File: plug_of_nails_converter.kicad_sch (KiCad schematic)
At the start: 6 parts, among them CN1 5103308-1

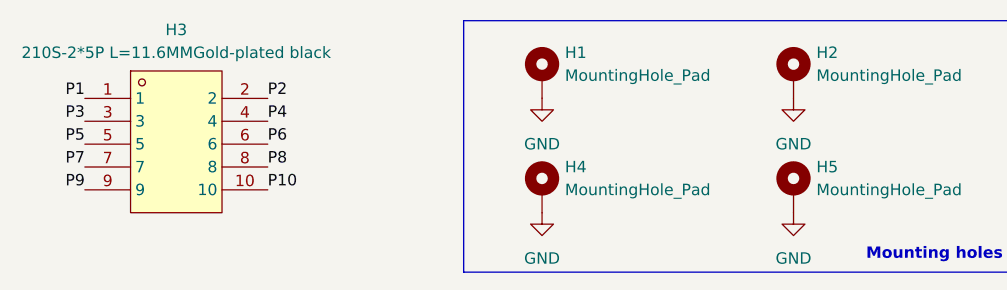
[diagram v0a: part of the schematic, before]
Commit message: Chaning IDC pin numbers and adding bottom CU layer
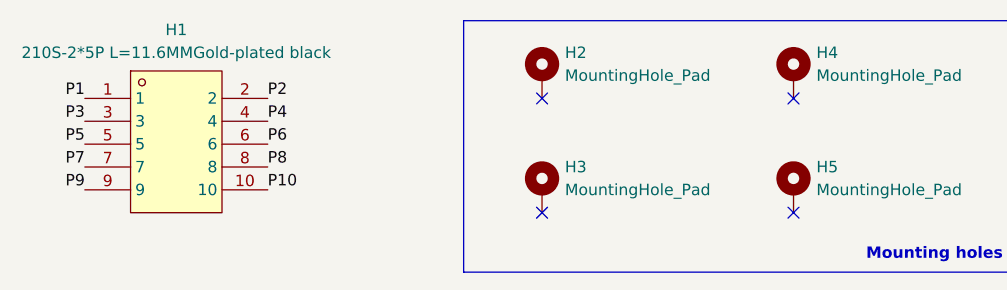
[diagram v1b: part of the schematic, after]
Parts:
- CN1: symbol my_symbol_library:5103308-1 -> pepy_sym_lib:[10P_2X5_IDC_MALE]TE Connectivity 5103308-1
- H1: renamed from H3; symbol my_symbol_library:210S-2*5PL=11.6MMGold-platedblack -> pepy_sym_lib:[10P_HEADER_STR]Ckmtw(Shenzhen Cankemeng) B-2100S10P-B110
- renumbered H1 to H2, H4 to H3, H2 to H4
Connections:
- removed net GND: H2.1, H3.1, H4.1, H5.1
- no-connect marks 0 -> 4

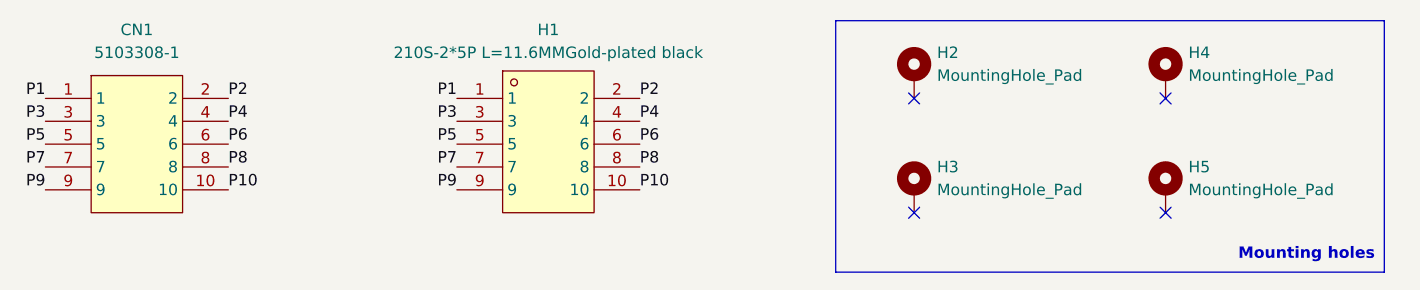
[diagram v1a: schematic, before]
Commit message: Updating symbols and testing kibot
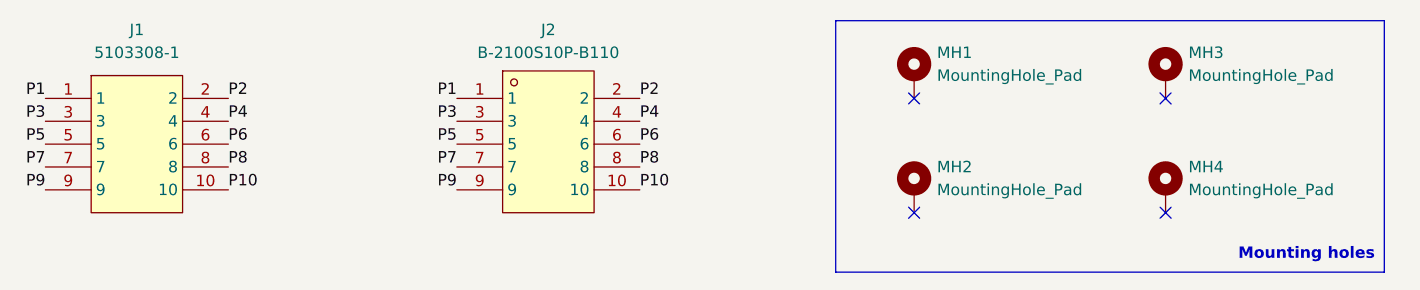
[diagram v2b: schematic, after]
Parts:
- J1: renamed from CN1; Manufacturer (none) -> TE Connectivity
- J2: renamed from H1; value 210S-2*5P L=11.6MMGold-plated black -> B-2100S10P-B110; Manufacturer (none) -> Ckmtw(Shenzhen Cankemeng)
- MH1: renamed from H2; symbol Mechanical:MountingHole_Pad -> pepy_sym_lib:[MOUNTING_HOLE]MountingHole_Pad; now left out of the parts list
- MH2: renamed from H3; symbol Mechanical:MountingHole_Pad -> pepy_sym_lib:[MOUNTING_HOLE]MountingHole_Pad; now left out of the parts list
- MH3: renamed from H4; symbol Mechanical:MountingHole_Pad -> pepy_sym_lib:[MOUNTING_HOLE]MountingHole_Pad; now left out of the parts list
- MH4: renamed from H5; symbol Mechanical:MountingHole_Pad -> pepy_sym_lib:[MOUNTING_HOLE]MountingHole_Pad; now left out of the parts list

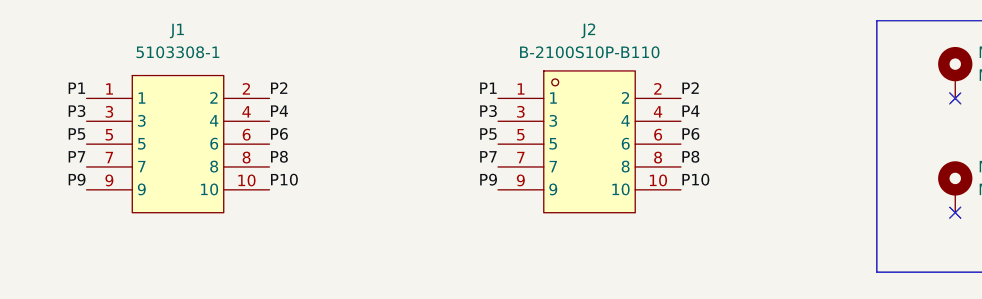
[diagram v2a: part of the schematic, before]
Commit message: Component library added as submodule
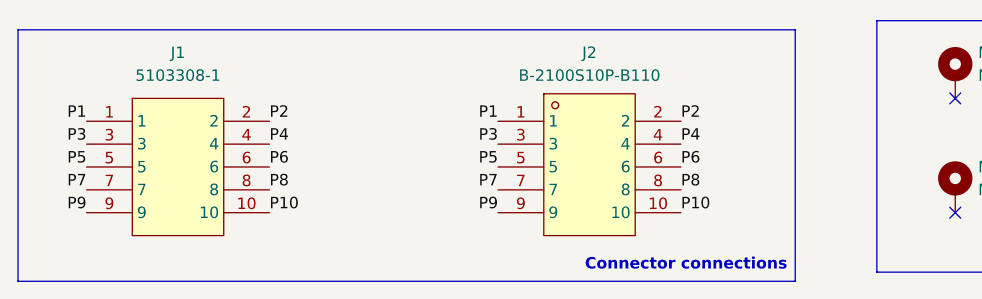
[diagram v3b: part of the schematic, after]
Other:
- note added: "Connector connections"
- company: (none) -> perseluspy
- title: (none) -> Plug of nails to pin header
- moved on the sheet: J1, J2

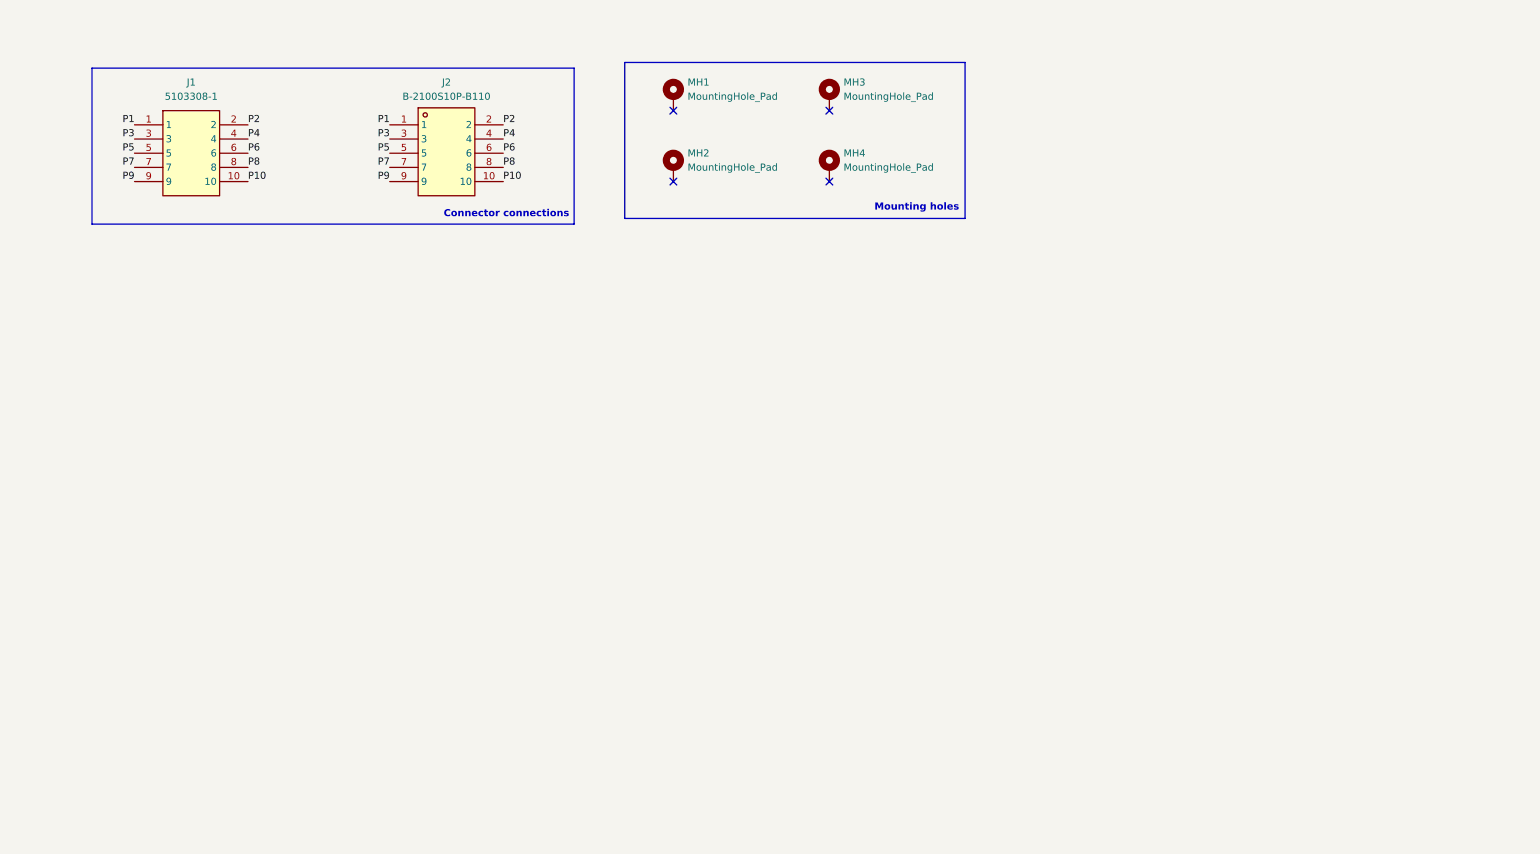
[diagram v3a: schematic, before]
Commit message: Version v3.0 with JLink Edu support
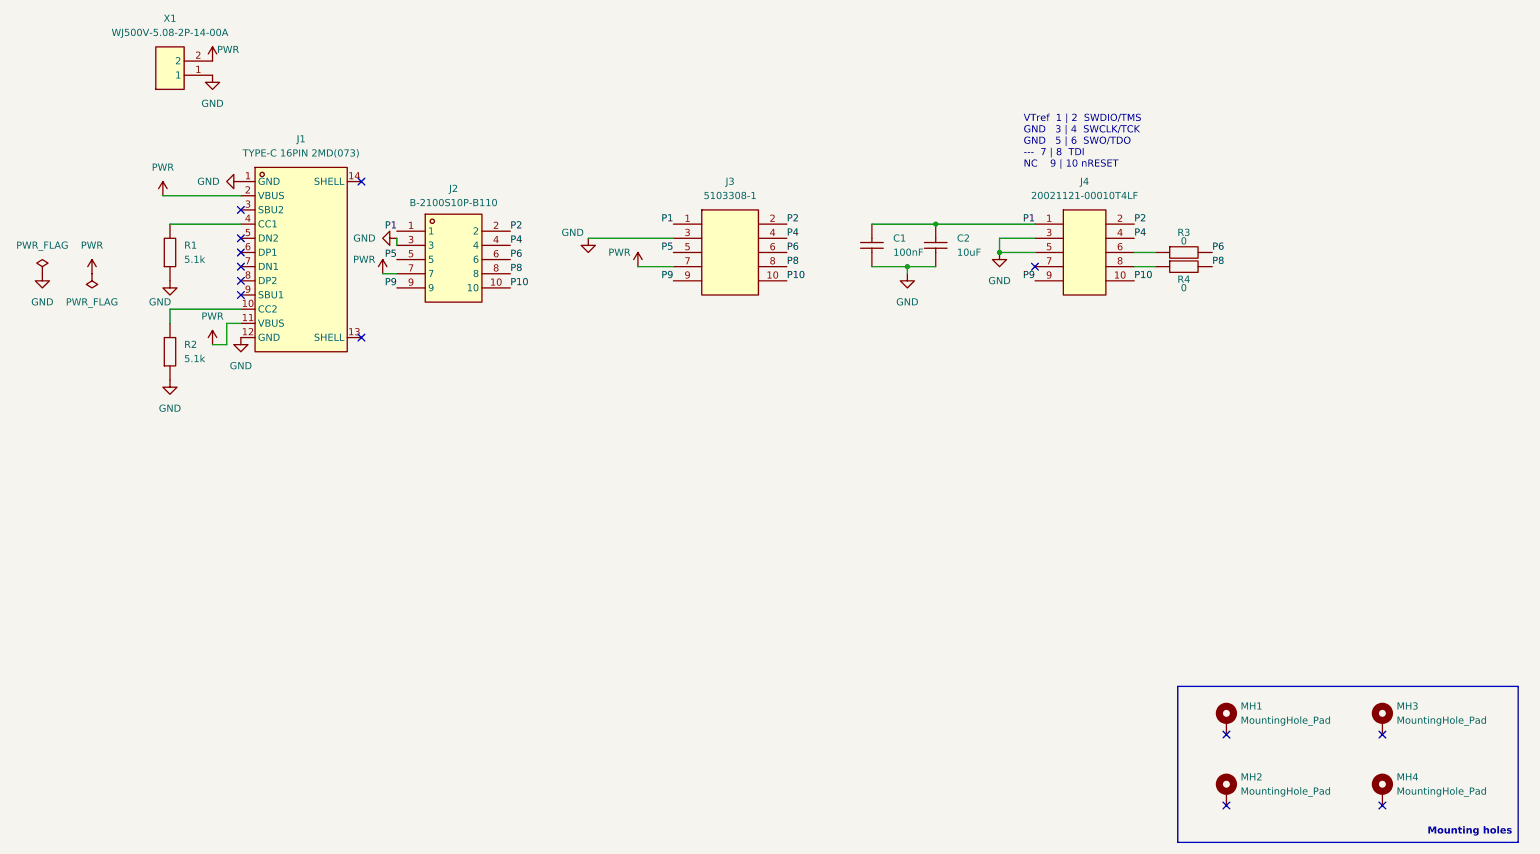
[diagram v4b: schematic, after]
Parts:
- removed J1: 5103308-1, pepy_sym_lib:[10P_2X5_IDC_MALE]TE Connectivity 5103308-1, symbol pepy_sym_lib:[10P_2X5_IDC_MALE]TE Connectivity 5103308-1
- added C1: CC0805KRX7R9BB104, pepy_sym_lib:[CAP_SMD_0805_2012Metric], symbol pepy_sym_lib:[CAP_SMD_0805_2012Metric]YAGEO CC0805KRX7R9BB104
- added C2: CL21A106KOQNNNE, pepy_sym_lib:[CAP_SMD_0805_2012Metric], symbol pepy_sym_lib:[CAP_SMD_0805_2012Metric]Samsung Electro-Mechanics CL21A106KOQNNNE
- added J1: TYPE-C 16PIN 2MD(073), pepy_sym_lib:[USB_C_16P_RA_FEMALE]SHOU HAN TYPE-C 16PIN 2MD(073), symbol pepy_sym_lib:[USB_C_16P_RA_FEMALE]SHOU HAN TYPE-C 16PIN 2MD(073)
- added J3: 5103308-1, pepy_sym_lib:[10P_2X5_IDC_MALE]TE Connectivity 5103308-1, symbol pepy_sym_lib:[10P_2X5_IDC_MALE]TE Connectivity 5103308-1
- added J4: 20021121-00010T4LF, pepy_sym_lib:[10P_2X5_IDC_1_27MM_MALE]Amphenol ICC 20021121-00010T4LF, symbol pepy_sym_lib:[10P_2X5_IDC_1_27MM_MALE]Amphenol ICC 20021121-00010T4LF
- added R1, R2: 0805W8F5101T5E, pepy_sym_lib:[RES_SMD_0805_2012Metric], symbol pepy_sym_lib:[RES_SMD_0805_2012Metric]UNI-ROYAL(Uniroyal Elec) 0805W8F5101T5E
- added R3, R4: 0805W8F0000T5E, pepy_sym_lib:[RES_SMD_0805_2012Metric], symbol pepy_sym_lib:[RES_SMD_0805_2012Metric]UNI-ROYAL(Uniroyal Elec) 0805W8F0000T5E
- added X1: WJ500V-5.08-2P-14-00A, pepy_sym_lib:[1x2_SCREW_TERMINAL_BLOCK]Ningbo Kangnex Elec WJ500V-5.08-2P, symbol pepy_sym_lib:[1x2_SCREW_TERMINAL_BLOCK]Ningbo Kangnex Elec WJ500V-5.08-2P
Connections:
- net P1: now also C1.2, C2.2, J3.1, J4.1
- net P10: now also J3.10, J4.10
- net P2: now also J3.2, J4.2
- net P4: now also J3.4, J4.4
- net P5: now also J3.5
- net P6: now also J3.6, R3.2
- net P8: now also J3.8, R4.2
- net P9: now also J3.9, J4.9
- net P3 renamed GND
- net GND: now also C1.1, C2.1, J1.1 (GND), J1.12 (GND), J3.3, J4.3, J4.5, R1.1, R2.1, X1.1
- net P7 renamed PWR
- net PWR: now also J1.11 (VBUS), J1.2 (VBUS), J3.7, X1.2
- new net: J4.6, R3.1
- new net: J1.10 (CC2), R2.2
- new net: J1.4 (CC1), R1.2
- new net: J4.8, R4.1
- no-connect marks 4 -> 13
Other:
- note added: "VTref 1 | 2 SWDIO/TMS GND 3 | 4 SWCLK/TCK GND 5 | 6 SWO/TDO --- 7 | 8 TDI NC 9 | 10 nRESET"
- note removed: "Connector connections"
- moved on the sheet: J2, MH1, MH2, MH3, MH4
